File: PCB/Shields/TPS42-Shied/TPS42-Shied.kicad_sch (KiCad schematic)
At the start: 6 parts, among them J1 PJ-320A, J2 Conn_01x06, J3 OLED, J4 PJ-320A, J5 Conn_01x06, J6 OLED

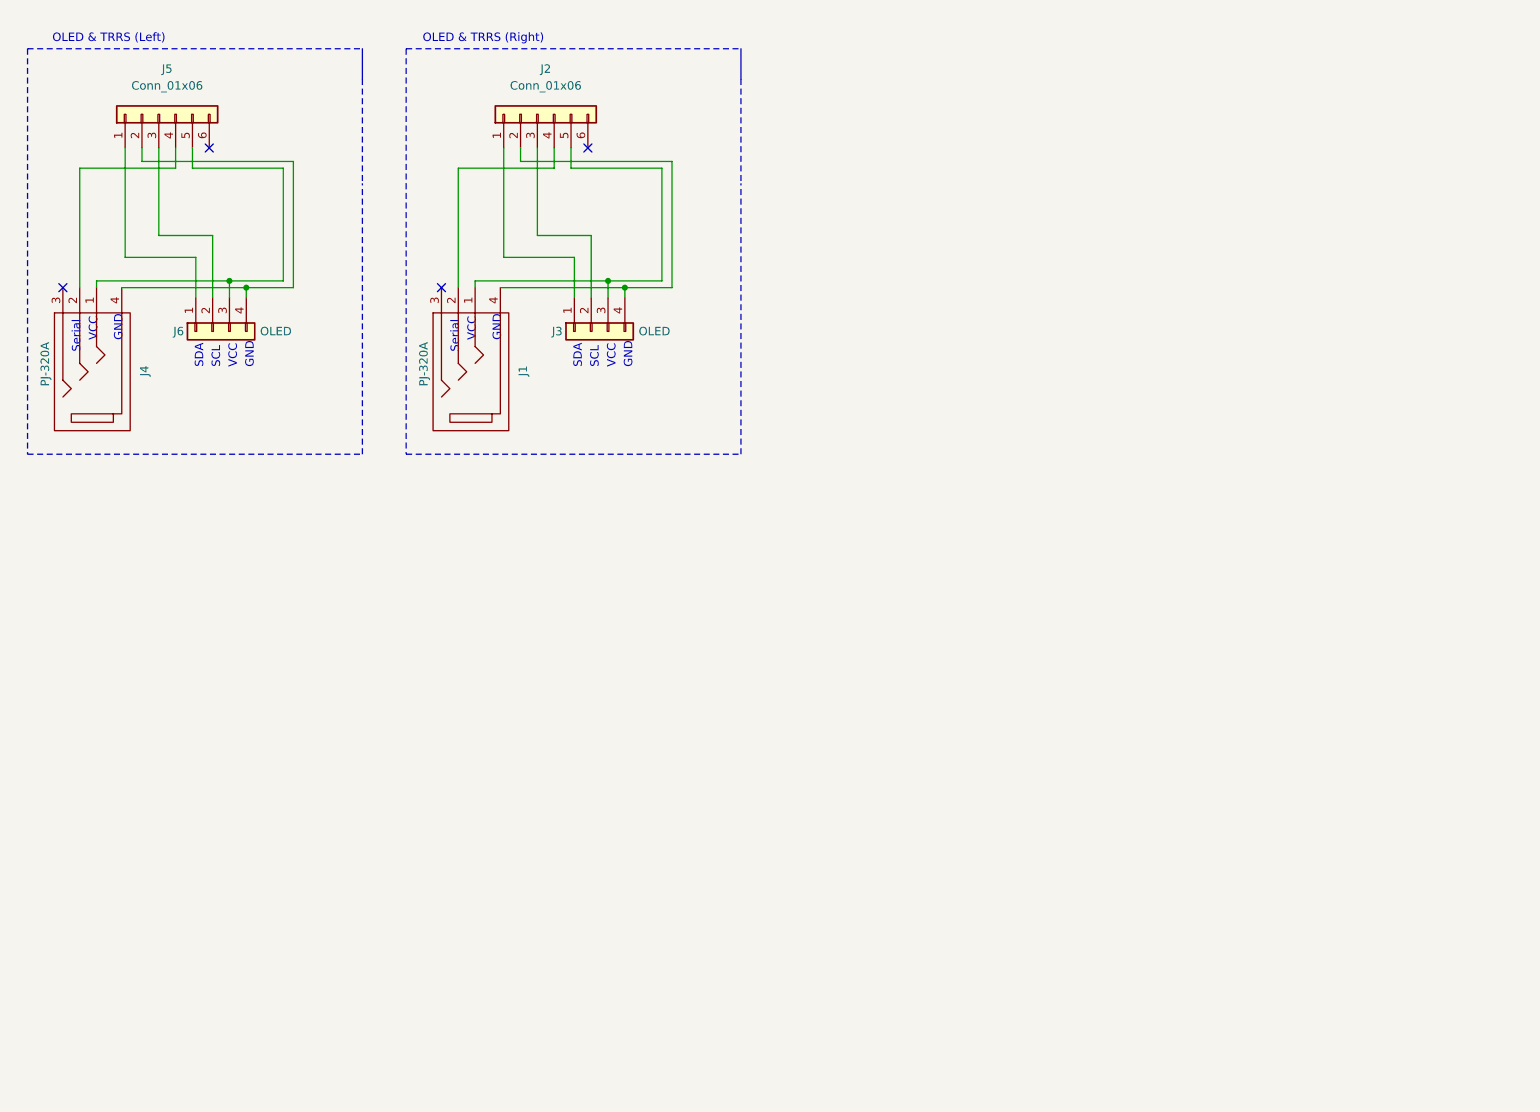
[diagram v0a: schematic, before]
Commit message: add left lcd shield
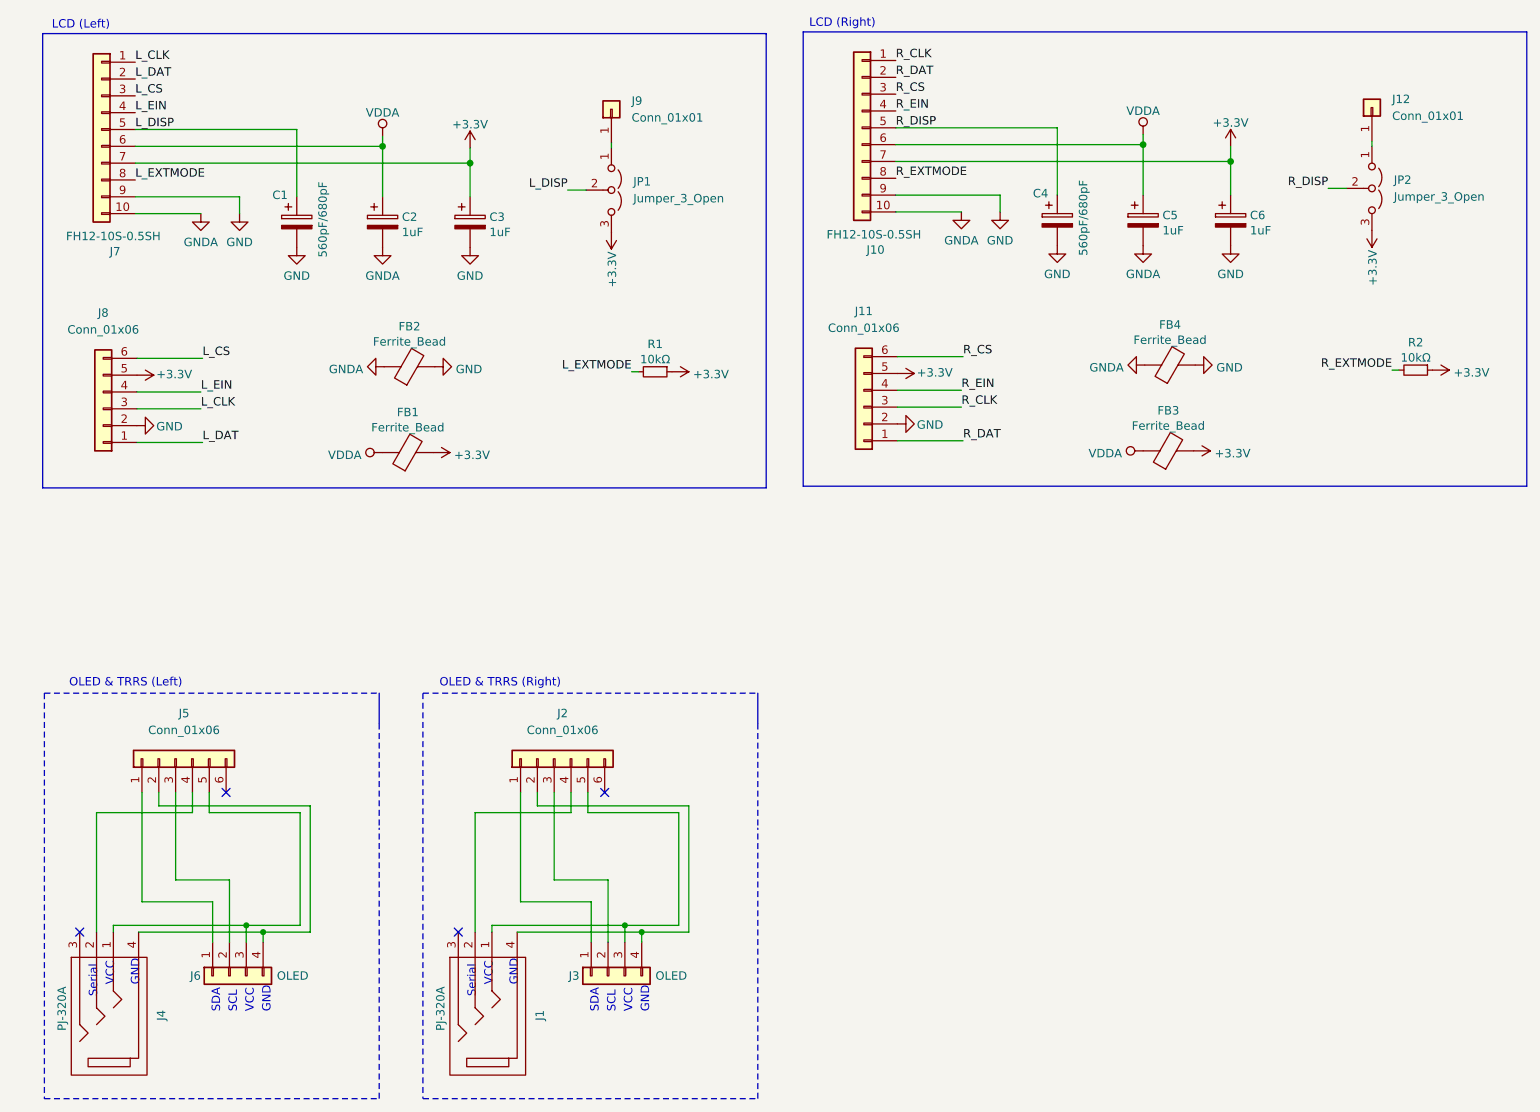
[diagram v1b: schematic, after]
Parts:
- added C1, C4: 560pF/680pF, Capacitor_SMD:C_0603_1608Metric_Pad1.08x0.95mm_HandSolder, symbol Device:CP
- added C2, C3, C5, C6: 1uF, Capacitor_SMD:C_0603_1608Metric_Pad1.08x0.95mm_HandSolder, symbol Device:CP
- added FB1, FB2, FB3, FB4: Ferrite_Bead, Resistor_SMD:R_0805_2012Metric_Pad1.20x1.40mm_HandSolder, symbol Device:Ferrite_Bead
- added J10, J7: FH12-10S-0.5SH, Connector_FFC-FPC:Hirose_FH12-10S-0.5SH_1x10-1MP_P0.50mm_Horizontal, symbol Connector_Generic:Conn_01x10
- added J11, J8: Conn_01x06, Connector_PinHeader_2.54mm:PinHeader_2x03_P2.54mm_Vertical, symbol Connector_Generic:Conn_01x06
- added J12, J9: Conn_01x01, Connector_PinHeader_2.54mm:PinHeader_1x01_P2.54mm_Vertical, symbol Connector_Generic:Conn_01x01
- added JP1, JP2: Jumper_3_Open, Jumper:SolderJumper-3_P2.0mm_Open_TrianglePad1.0x1.5mm, symbol Jumper:Jumper_3_Open
- added R1, R2: 10kΩ, Resistor_SMD:R_0603_1608Metric_Pad0.98x0.95mm_HandSolder, symbol Device:R_Small
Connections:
- new net: J12.1 (Pin_1), JP2.1 (A)
- new net: J9.1 (Pin_1), JP1.1 (A)
- new net +3V3: C3.1, C6.1, FB1.2, FB3.2, J10.7 (Pin_7), J11.5 (Pin_5), J7.7 (Pin_7), J8.5 (Pin_5), JP1.3 (B), JP2.3 (B), R1.1, R2.1
- new net GND: C1.2, C3.2, C4.2, C6.2, FB2.2, FB4.2, J10.9 (Pin_9), J11.2 (Pin_2), J7.9 (Pin_9), J8.2 (Pin_2)
- new net GNDA: C2.2, C5.2, FB2.1, FB4.1, J10.10 (Pin_10), J7.10 (Pin_10)
- new net L_CLK: J7.1 (Pin_1), J8.3 (Pin_3)
- new net L_CS: J7.3 (Pin_3), J8.6 (Pin_6)
- new net L_DAT: J7.2 (Pin_2), J8.1 (Pin_1)
- new net L_DISP: C1.1, J7.5 (Pin_5), JP1.2 (C)
- new net L_EIN: J7.4 (Pin_4), J8.4 (Pin_4)
- new net L_EXTMODE: J7.8 (Pin_8), R1.2
- new net R_CLK: J10.1 (Pin_1), J11.3 (Pin_3)
- new net R_CS: J10.3 (Pin_3), J11.6 (Pin_6)
- new net R_DAT: J10.2 (Pin_2), J11.1 (Pin_1)
- new net R_DISP: C4.1, J10.5 (Pin_5), JP2.2 (C)
- new net R_EIN: J10.4 (Pin_4), J11.4 (Pin_4)
- new net R_EXTMODE: J10.8 (Pin_8), R2.2
- new net VDDA: C2.1, C5.1, FB1.1, FB3.1, J10.6 (Pin_6), J7.6 (Pin_6)
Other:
- note added: "LCD (Left)"
- note added: "LCD (Right)"
- moved on the sheet: J1, J2, J3, J4, J5, J6
